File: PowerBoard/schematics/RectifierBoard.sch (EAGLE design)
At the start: 9 parts, among them J1 POWER_JACKPTH, X1 22-27-2031-03, X2 22-27-2031-03

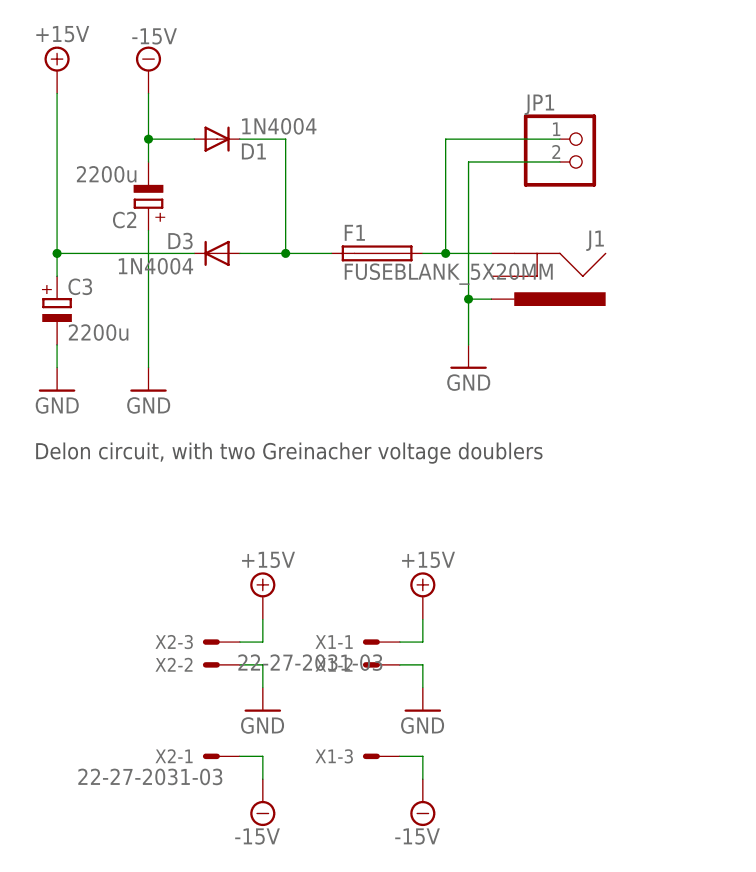
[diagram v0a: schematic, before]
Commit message: added fuse, realistically sized capacitor footprints
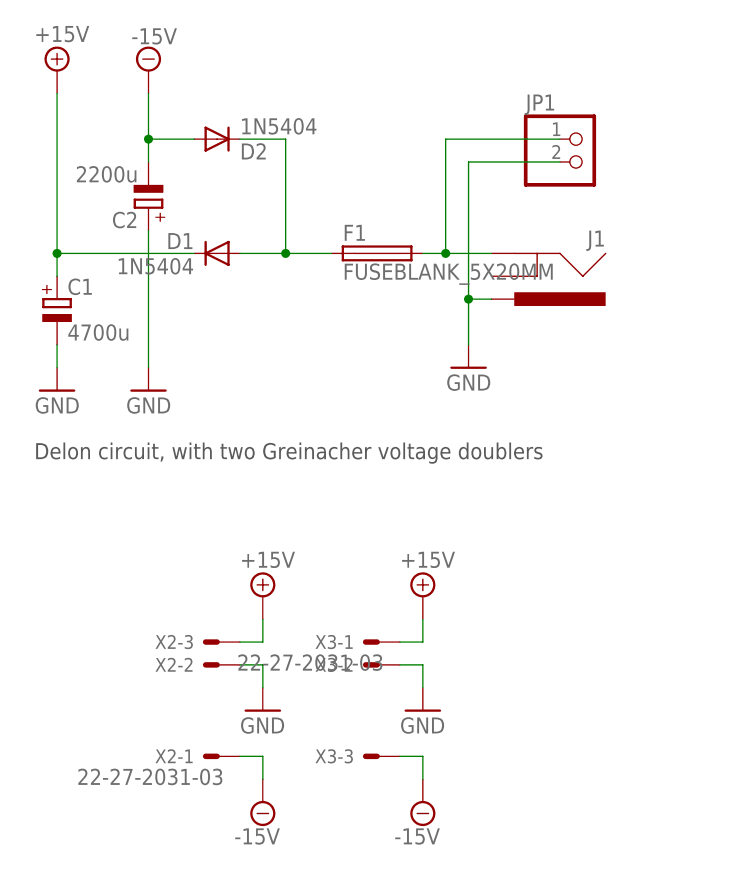
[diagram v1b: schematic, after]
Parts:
- removed C3: 2200u, rcl:CPOL-EUE5-10.5
- removed D3: 1N4004, Rebel:DIODE1N4001
- added C1: 4700u, resistor:CPOL-EUE7.5-18
- added D2: 1N5404, Rebel:DIODE1N4001
- C2: device rcl:CPOL-EUE5-10.5 -> resistor:CPOL-EUE7.5-18
- D1: value 1N4004 -> 1N5404
- renumbered X1 to X3
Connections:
- net +15V: now also C1.+, D1.C; no longer C3.+, D3.C
- net -15V: now also D2.A; no longer D1.A
- net GND: now also C1.-; no longer C3.-
- net N$1: now also D1.A, D2.C; no longer D1.C, D3.A
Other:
- moved on the sheet: D1
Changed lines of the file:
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@@
 </classes>
 <parts>
-<part name="X1" library="con-molex" deviceset="22-?-03" device="27-2031"/>
 <part name="SUPPLY2" library="supply2" deviceset="-15V" device=""/>
 <part name="SUPPLY4" library="supply2" deviceset="+15V" device=""/>
@@
 <part name="GND1" library="supply1" deviceset="GND" device=""/>
 <part name="GND2" library="supply1" deviceset="GND" device=""/>
-<part name="C2" library="rcl" deviceset="CPOL-EU" device="E5-10.5" value="2200u"/>
-<part name="C3" library="rcl" deviceset="CPOL-EU" device="E5-10.5" value="2200u"/>
-<part name="D3" library="Rebel" deviceset="DIODE" device="1N4001" value="1N4004"/>
+<part name="C2" library="resistor" deviceset="CPOL-EU" device="E7.5-18" value="2200u"/>
+<part name="C1" library="resistor" deviceset="CPOL-EU" device="E7.5-18" value="4700u"/>
+<part name="D1" library="Rebel" deviceset="DIODE" device="1N4001" value="1N5404"/>
 <part name="J1" library="SparkFun" deviceset="POWER_JACK" device="PTH" value=""/>
 <part name="GND8" library="supply1" deviceset="GND" device=""/>
-<part name="D1" library="Rebel" deviceset="DIODE" device="1N4001" value="1N4004"/>
+<part name="D2" library="Rebel" deviceset="DIODE" device="1N4001" value="1N5404"/>
 <part name="GND3" library="supply1" deviceset="GND" device=""/>
 <part name="GND4" library="supply1" deviceset="GND" device=""/>
@@
 <part name="JP1" library="pinhead" deviceset="PINHD-1X2" device=""/>
 <part name="F1" library="fuse" deviceset="FUSE" device="BLANK_5X20MM"/>
+<part name="X3" library="con-molex" deviceset="22-?-03" device="27-2031"/>
 </parts>
 <sheets>
@@
 </plain>
 <instances>
-<instance part="X1" gate="-1" x="38.1" y="33.02" rot="R180"/>
-<instance part="X1" gate="-2" x="38.1" y="30.48" rot="R180"/>
-<instance part="X1" gate="-3" x="38.1" y="20.32" rot="R180"/>
 <instance part="SUPPLY2" gate="G$1" x="43.18" y="15.24"/>
 <instance part="SUPPLY4" gate="+15V" x="43.18" y="38.1"/>
@@
 <instance part="GND2" gate="1" x="43.18" y="25.4"/>
 <instance part="C2" gate="G$1" x="12.7" y="81.28" rot="R180"/>
-<instance part="C3" gate="G$1" x="2.54" y="71.12"/>
-<instance part="D3" gate="G$1" x="20.32" y="76.2" rot="MR0"/>
+<instance part="C1" gate="G$1" x="2.54" y="71.12"/>
+<instance part="D1" gate="G$1" x="20.32" y="76.2" rot="MR0"/>
 <instance part="J1" gate="G$1" x="53.34" y="78.74" rot="R180"/>
 <instance part="GND8" gate="1" x="48.26" y="63.5" rot="MR0"/>
-<instance part="D1" gate="G$1" x="20.32" y="88.9" rot="MR180"/>
+<instance part="D2" gate="G$1" x="20.32" y="88.9" rot="MR180"/>
 <instance part="GND3" gate="1" x="12.7" y="60.96" rot="MR0"/>
 <instance part="GND4" gate="1" x="2.54" y="60.96" rot="MR0"/>
@@
 <instance part="JP1" gate="G$1" x="60.96" y="86.36"/>
 <instance part="F1" gate="G$1" x="38.1" y="76.2"/>
+<instance part="X3" gate="-1" x="38.1" y="33.02" rot="R180"/>
+<instance part="X3" gate="-2" x="38.1" y="30.48" rot="R180"/>
+<instance part="X3" gate="-3" x="38.1" y="20.32" rot="R180"/>
 </instances>
 <busses>
@@
 <pinref part="SUPPLY4" gate="+15V" pin="+15V"/>
 <wire x1="43.18" y1="33.02" x2="43.18" y2="35.56" width="0.1524" layer="91"/>
-<pinref part="X1" gate="-1" pin="S"/>
-<wire x1="40.64" y1="33.02" x2="43.18" y2="33.02" width="0.1524" layer="91"/>
+<pinref part="X3" gate="-1" pin="S"/>
+<wire x1="43.18" y1="33.02" x2="40.64" y2="33.02" width="0.1524" layer="91"/>
 </segment>
 <segment>
@@
 </segment>
 <segment>
-<pinref part="D3" gate="G$1" pin="C"/>
-<pinref part="C3" gate="G$1" pin="+"/>
+<pinref part="D1" gate="G$1" pin="C"/>
+<pinref part="C1" gate="G$1" pin="+"/>
 <wire x1="17.78" y1="76.2" x2="2.54" y2="76.2" width="0.1524" layer="91"/>
 <wire x1="2.54" y1="76.2" x2="2.54" y2="73.66" width="0.1524" layer="91"/>
@@
 <pinref part="SUPPLY2" gate="G$1" pin="-15V"/>
 <wire x1="43.18" y1="20.32" x2="43.18" y2="17.78" width="0.1524" layer="91"/>
-<pinref part="X1" gate="-3" pin="S"/>
+<pinref part="X3" gate="-3" pin="S"/>
 <wire x1="40.64" y1="20.32" x2="43.18" y2="20.32" width="0.1524" layer="91"/>
 </segment>
@@
 </segment>
 <segment>
-<pinref part="D1" gate="G$1" pin="A"/>
+<pinref part="D2" gate="G$1" pin="A"/>
 <wire x1="17.78" y1="88.9" x2="12.7" y2="88.9" width="0.1524" layer="91"/>
 <pinref part="C2" gate="G$1" pin="-"/>
@@
 </segment>
 <segment>
-<pinref part="X1" gate="-2" pin="S"/>
-<wire x1="40.64" y1="30.48" x2="43.18" y2="30.48" width="0.1524" layer="91"/>
 <wire x1="43.18" y1="30.48" x2="43.18" y2="27.94" width="0.1524" layer="91"/>
 <pinref part="GND2" gate="1" pin="GND"/>
+<pinref part="X3" gate="-2" pin="S"/>
+<wire x1="40.64" y1="30.48" x2="43.18" y2="30.48" width="0.1524" layer="91"/>
 </segment>
 <segment>
@@
 </segment>
 <segment>
-<pinref part="C3" gate="G$1" pin="-"/>
+<pinref part="C1" gate="G$1" pin="-"/>
 <pinref part="GND4" gate="1" pin="GND"/>
 <wire x1="2.54" y1="63.5" x2="2.54" y2="66.04" width="0.1524" layer="91"/>
@@
 <net name="N$1" class="0">
 <segment>
-<pinref part="D3" gate="G$1" pin="A"/>
+<pinref part="D1" gate="G$1" pin="A"/>
 <wire x1="22.86" y1="76.2" x2="27.94" y2="76.2" width="0.1524" layer="91"/>
-<pinref part="D1" gate="G$1" pin="C"/>
+<pinref part="D2" gate="G$1" pin="C"/>
 <wire x1="27.94" y1="76.2" x2="33.02" y2="76.2" width="0.1524" layer="91"/>
 <wire x1="22.86" y1="88.9" x2="27.94" y2="88.9" width="0.1524" layer="91"/>
